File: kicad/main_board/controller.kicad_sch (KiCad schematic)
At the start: 44 parts, among them J6 FRONT_PANEL, J7 I2C, J8 SWD, U7 MCP4728, U8 RP2040, U9 W25Q128JVP, Y1 12MHz

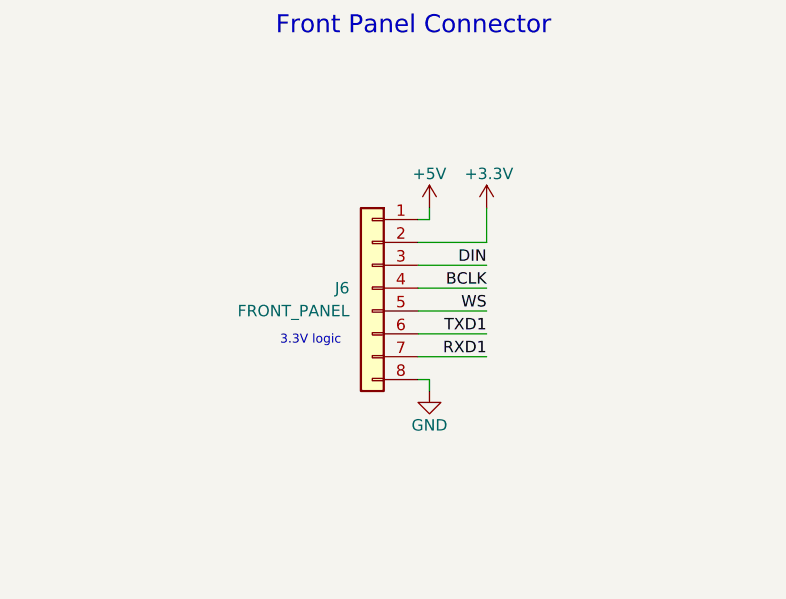
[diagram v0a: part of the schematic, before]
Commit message: use 2x4 IDC connector
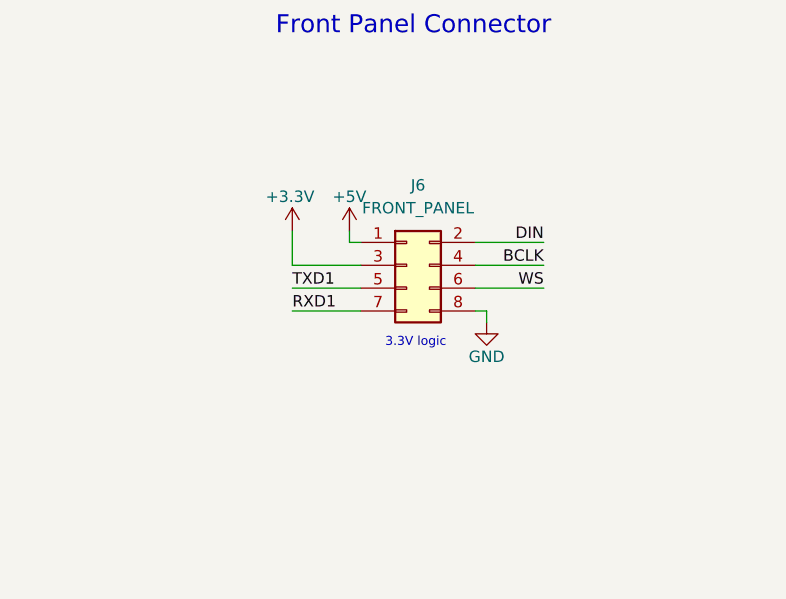
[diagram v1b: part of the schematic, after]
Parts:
- J6: footprint Connector_JST:JST_XH_B8B-XH-A_1x08_P2.50mm_Vertical -> Connector_IDC:IDC-Header_2x04_P2.54mm_Vertical; symbol Connector_Generic:Conn_01x08 -> Connector_Generic:Conn_02x04_Odd_Even; LCSC C7429638 -> C5372864
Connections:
- net +3.3V: now also J6.3 (Pin_3); no longer J6.2 (Pin_2)
- net DIN: now also J6.2 (Pin_2); no longer J6.3 (Pin_3)
- net TXD1: now also J6.5 (Pin_5); no longer J6.6 (Pin_6)
- net WS: now also J6.6 (Pin_6); no longer J6.5 (Pin_5)
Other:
- moved on the sheet: J6
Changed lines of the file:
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@@
 	(title_block
 		(title "SW32 - Main Board")
-		(date "2024-05-23")
+		(date "2024-05-29")
 		(rev "1")
 		(company "saawsm")
@@
 	(wire
 		(pts
-			(xy 58.42 45.72) (xy 58.42 46.99)
+			(xy 49.53 48.26) (xy 49.53 49.53)
 		)
 		(stroke
@@
 	(wire
 		(pts
-			(xy 64.77 45.72) (xy 64.77 49.53)
+			(xy 43.18 48.26) (xy 43.18 52.07)
 		)
 		(stroke
@@
 	(wire
 		(pts
-			(xy 57.15 62.23) (xy 64.77 62.23)
+			(xy 50.8 57.15) (xy 43.18 57.15)
 		)
 		(stroke
@@
 	(wire
 		(pts
-			(xy 57.15 57.15) (xy 64.77 57.15)
+			(xy 63.5 54.61) (xy 71.12 54.61)
 		)
 		(stroke
@@
 	(wire
 		(pts
-			(xy 64.77 49.53) (xy 57.15 49.53)
+			(xy 43.18 52.07) (xy 50.8 52.07)
 		)
 		(stroke
@@
 	(wire
 		(pts
-			(xy 57.15 52.07) (xy 64.77 52.07)
+			(xy 63.5 49.53) (xy 71.12 49.53)
 		)
 		(stroke
@@
 	(wire
 		(pts
-			(xy 57.15 54.61) (xy 64.77 54.61)
+			(xy 63.5 52.07) (xy 71.12 52.07)
 		)
 		(stroke
@@
 	(wire
 		(pts
-			(xy 58.42 64.77) (xy 58.42 66.04)
+			(xy 64.77 57.15) (xy 64.77 58.42)
 		)
 		(stroke
@@
 	(wire
 		(pts
-			(xy 57.15 59.69) (xy 64.77 59.69)
+			(xy 50.8 54.61) (xy 43.18 54.61)
 		)
 		(stroke
@@
 	(wire
 		(pts
-			(xy 58.42 64.77) (xy 57.15 64.77)
+			(xy 64.77 57.15) (xy 63.5 57.15)
 		)
 		(stroke
@@
 	(wire
 		(pts
-			(xy 57.15 46.99) (xy 58.42 46.99)
+			(xy 50.8 49.53) (xy 49.53 49.53)
 		)
 		(stroke
@@
 	(text "3.3V logic"
 		(exclude_from_sim no)
-		(at 45.212 60.452 0)
+		(at 56.896 60.706 0)
 		(effects
 			(font
@@
 	)
 	(label "WS"
-		(at 64.77 57.15 180)
+		(at 71.12 54.61 180)
 		(fields_autoplaced yes)
 		(effects
@@
 	)
 	(label "DIN"
-		(at 64.77 52.07 180)
+		(at 71.12 49.53 180)
 		(fields_autoplaced yes)
 		(effects
@@
 	)
 	(label "TXD1"
-		(at 64.77 59.69 180)
+		(at 43.18 54.61 0)
 		(fields_autoplaced yes)
 		(effects
@@
 				(size 1.27 1.27)
 			)
-			(justify right bottom)
+			(justify left bottom)
 		)
 	)
@@
 	)
 	(label "RXD1"
-		(at 64.77 62.23 180)
+		(at 43.18 57.15 0)
 		(fields_autoplaced yes)
 		(effects
@@
 				(size 1.27 1.27)
 			)
-			(justify right bottom)
+			(justify left bottom)
 		)
 	)
@@
 	)
 	(label "BCLK"
-		(at 64.77 54.61 180)
+		(at 71.12 52.07 180)
 		(fields_autoplaced yes)
 		(effects
@@
 	)
 	(symbol
-		(lib_id "Connector_Generic:Conn_01x08")
-		(at 52.07 54.61 0)
-		(mirror y)
+		(lib_id "Connector_Generic:Conn_02x04_Odd_Even")
+		(at 55.88 52.07 0)
 		(unit 1)
 		(exclude_from_sim no)
@@
 		(on_board yes)
 		(dnp no)
-		(fields_autoplaced yes)
 		(property "Reference" "J6"
-			(at 49.53 54.6099 0)
+			(at 57.15 43.18 0)
 			(effects
 				(font
 					(size 1.27 1.27)
 				)
-				(justify left)
 			)
 		)
 		(property "Value" "FRONT_PANEL"
-			(at 49.53 57.1499 0)
+			(at 57.15 45.72 0)
 			(effects
 				(font
 					(size 1.27 1.27)
 				)
-				(justify left)
 			)
 		)
-		(property "Footprint" "Connector_JST:JST_XH_B8B-XH-A_1x08_P2.50mm_Vertical"
-			(at 52.07 54.61 0)
+		(property "Footprint" "Connector_IDC:IDC-Header_2x04_P2.54mm_Vertical"
+			(at 55.88 52.07 0)
 			(effects
 				(font
@@
 			)
 		)
-		(property "Datasheet" "~"
-			(at 52.07 54.61 0)
+		(property "Datasheet" "https://www.lcsc.com/datasheet/lcsc_datasheet_2303141000_HCTL-HC-JN254-2-04-Z_C5372864.pdf"
+			(at 55.88 52.07 0)
 			(effects
 				(font
@@
 			)
 		)
-		(property "Description" "Generic connector, single row, 01x08, script generated (kicad-library-utils/schlib/autogen/connector/)"
-			(at 52.07 54.61 0)
+		(property "Description" "Generic connector, double row, 02x04, odd/even pin numbering scheme (row 1 odd numbers, row 2 even numbers), script generated (kicad-library-utils/schlib/autogen/connector/)"
+			(at 55.88 52.07 0)
 			(effects
 				(font
@@
 			)
 		)
-		(property "LCSC" "C7429638"
-			(at 52.07 54.61 0)
+		(property "LCSC" "C5372864"
+			(at 55.88 52.07 0)
 			(effects
 				(font
@@
 		)
 		(property "Service" "HandAssembly"
-			(at 52.07 54.61 0)
+			(at 55.88 52.07 0)
 			(effects
 				(font
@@
 	(symbol
 		(lib_id "power:+3.3V")
-		(at 64.77 45.72 0)
-		(mirror y)
+		(at 43.18 48.26 0)
 		(unit 1)
 		(exclude_from_sim no)
@@
 		(dnp no)
 		(property "Reference" "#PWR0102"
-			(at 64.77 49.53 0)
+			(at 43.18 52.07 0)
 			(effects
 				(font
@@
 		)
 		(property "Value" "+3.3V"
-			(at 65.024 41.91 0)
+			(at 42.926 44.45 0)
 			(effects
 				(font
@@
 		)
 		(property "Footprint" ""
-			(at 64.77 45.72 0)
+			(at 43.18 48.26 0)
 			(effects
 				(font
@@
 		)
 		(property "Datasheet" ""
-			(at 64.77 45.72 0)
+			(at 43.18 48.26 0)
 			(effects
 				(font
@@
 		)
 		(property "Description" "Power symbol creates a global label with name \"+3.3V\""
-			(at 64.77 45.72 0)
+			(at 43.18 48.26 0)
 			(effects
 				(font
@@
 	(symbol
 		(lib_id "power:+5V")
-		(at 58.42 45.72 0)
+		(at 49.53 48.26 0)
+		(mirror y)
 		(unit 1)
 		(exclude_from_sim no)
@@
 		(dnp no)
 		(property "Reference" "#PWR0100"
-			(at 58.42 49.53 0)
+			(at 49.53 52.07 0)
 			(effects
 				(font
@@
 		)
 		(property "Value" "+5V"
-			(at 58.42 41.91 0)
+			(at 49.53 44.45 0)
 			(effects
 				(font
@@
 		)
 		(property "Footprint" ""
-			(at 58.42 45.72 0)
+			(at 49.53 48.26 0)
 			(effects
 				(font
@@
 		)
 		(property "Datasheet" ""
-			(at 58.42 45.72 0)
+			(at 49.53 48.26 0)
 			(effects
 				(font
@@
 		)
 		(property "Description" "Power symbol creates a global label with name \"+5V\""
-			(at 58.42 45.72 0)
+			(at 49.53 48.26 0)
 			(effects
 				(font
@@
 	(symbol
 		(lib_id "power:GND")
-		(at 58.42 66.04 0)
+		(at 64.77 58.42 0)
 		(mirror y)
 		(unit 1)
@@
 		(dnp no)
 		(property "Reference" "#PWR0101"
-			(at 58.42 72.39 0)
+			(at 64.77 64.77 0)
 			(effects
 				(font
@@
 		)
 		(property "Value" "GND"
-			(at 58.42 69.85 0)
+			(at 64.77 62.23 0)
 			(effects
 				(font
@@
 		)
 		(property "Footprint" ""
-			(at 58.42 66.04 0)
+			(at 64.77 58.42 0)
 			(effects
 				(font
@@
 		)
 		(property "Datasheet" ""
-			(at 58.42 66.04 0)
+			(at 64.77 58.42 0)
 			(effects
 				(font
@@
 		)
 		(property "Description" "Power symbol creates a global label with name \"GND\" , ground"
-			(at 58.42 66.04 0)
+			(at 64.77 58.42 0)
 			(effects
 				(font

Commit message: connect charger VBUS before inrush limiter
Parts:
- renumbered R45 to R50, R46 to R51, R47 to R52, R48 to R53, R49 to R54, R50 to R55, R51 to R56, R52 to R57, R53 to R58, R54 to R59, R55 to R60, R56 to R61
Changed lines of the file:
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@@
 	(title_block
 		(title "SW32 - Main Board")
-		(date "2024-05-29")
+		(date "2024-05-31")
 		(rev "1")
 		(company "saawsm")
@@
 		(dnp no)
 		(fields_autoplaced yes)
-		(property "Reference" "R51"
+		(property "Reference" "R56"
 			(at 154.94 180.3399 0)
 			(effects
@@
 			(project "main_board"
 				(path "/8e1f1504-76c2-49e6-9261-3c1190503f8c/c17fbfa0-81d7-4817-8752-da6de21e6518"
-					(reference "R51")
+					(reference "R56")
 					(unit 1)
 				)
@@
 		(dnp no)
 		(fields_autoplaced yes)
-		(property "Reference" "R50"
+		(property "Reference" "R55"
 			(at 128.27 60.9599 0)
 			(effects
@@
 			(project "main_board"
 				(path "/8e1f1504-76c2-49e6-9261-3c1190503f8c/c17fbfa0-81d7-4817-8752-da6de21e6518"
-					(reference "R50")
+					(reference "R55")
 					(unit 1)
 				)
@@
 		(on_board yes)
 		(dnp no)
-		(property "Reference" "R45"
+		(property "Reference" "R50"
 			(at 41.148 146.05 0)
 			(effects
@@
 			(project "main_board"
 				(path "/8e1f1504-76c2-49e6-9261-3c1190503f8c/c17fbfa0-81d7-4817-8752-da6de21e6518"
-					(reference "R45")
+					(reference "R50")
 					(unit 1)
 				)
@@
 		(on_board yes)
 		(dnp no)
-		(property "Reference" "R55"
+		(property "Reference" "R60"
 			(at 270.51 42.926 90)
 			(effects
@@
 			(project "main_board"
 				(path "/8e1f1504-76c2-49e6-9261-3c1190503f8c/c17fbfa0-81d7-4817-8752-da6de21e6518"
-					(reference "R55")
+					(reference "R60")
 					(unit 1)
 				)
@@
 		(on_board yes)
 		(dnp no)
-		(property "Reference" "#PWR0102"
+		(property "Reference" "#PWR098"
 			(at 43.18 52.07 0)
 			(effects
@@
 			(project "main_board"
 				(path "/8e1f1504-76c2-49e6-9261-3c1190503f8c/c17fbfa0-81d7-4817-8752-da6de21e6518"
-					(reference "#PWR0102")
+					(reference "#PWR098")
 					(unit 1)
 				)
@@
 		(on_board yes)
 		(dnp no)
-		(property "Reference" "#PWR0100"
+		(property "Reference" "#PWR0101"
 			(at 49.53 52.07 0)
 			(effects
@@
 			(project "main_board"
 				(path "/8e1f1504-76c2-49e6-9261-3c1190503f8c/c17fbfa0-81d7-4817-8752-da6de21e6518"
-					(reference "#PWR0100")
+					(reference "#PWR0101")
 					(unit 1)
 				)
@@
 		(dnp no)
 		(fields_autoplaced yes)
-		(property "Reference" "R52"
+		(property "Reference" "R57"
 			(at 166.37 180.3399 0)
 			(effects
@@
 			(project "main_board"
 				(path "/8e1f1504-76c2-49e6-9261-3c1190503f8c/c17fbfa0-81d7-4817-8752-da6de21e6518"
-					(reference "R52")
+					(reference "R57")
 					(unit 1)
 				)
@@
 		(on_board yes)
 		(dnp no)
-		(property "Reference" "#PWR0101"
+		(property "Reference" "#PWR0102"
 			(at 64.77 64.77 0)
 			(effects
@@
 			(project "main_board"
 				(path "/8e1f1504-76c2-49e6-9261-3c1190503f8c/c17fbfa0-81d7-4817-8752-da6de21e6518"
-					(reference "#PWR0101")
+					(reference "#PWR0102")
 					(unit 1)
 				)
@@
 		(on_board yes)
 		(dnp no)
-		(property "Reference" "R53"
+		(property "Reference" "R58"
 			(at 207.01 52.07 0)
 			(effects
@@
 			(project "main_board"
 				(path "/8e1f1504-76c2-49e6-9261-3c1190503f8c/c17fbfa0-81d7-4817-8752-da6de21e6518"
-					(reference "R53")
+					(reference "R58")
 					(unit 1)
 				)
@@
 		(on_board yes)
 		(dnp no)
-		(property "Reference" "#PWR098"
+		(property "Reference" "#PWR099"
 			(at 46.99 181.61 0)
 			(effects
@@
 			(project "main_board"
 				(path "/8e1f1504-76c2-49e6-9261-3c1190503f8c/c17fbfa0-81d7-4817-8752-da6de21e6518"
-					(reference "#PWR098")
+					(reference "#PWR099")
 					(unit 1)
 				)
@@
 		(dnp no)
 		(fields_autoplaced yes)
-		(property "Reference" "R56"
+		(property "Reference" "R61"
 			(at 273.05 77.4699 0)
 			(effects
@@
 			(project "main_board"
 				(path "/8e1f1504-76c2-49e6-9261-3c1190503f8c/c17fbfa0-81d7-4817-8752-da6de21e6518"
-					(reference "R56")
+					(reference "R61")
 					(unit 1)
 				)
@@
 		(on_board yes)
 		(dnp no)
-		(property "Reference" "R49"
+		(property "Reference" "R54"
 			(at 124.46 79.502 90)
 			(effects
@@
 			(project "main_board"
 				(path "/8e1f1504-76c2-49e6-9261-3c1190503f8c/c17fbfa0-81d7-4817-8752-da6de21e6518"
-					(reference "R49")
+					(reference "R54")
 					(unit 1)
 				)
@@
 		(on_board yes)
 		(dnp no)
-		(property "Reference" "#PWR099"
+		(property "Reference" "#PWR0100"
 			(at 48.26 146.05 0)
 			(effects
@@
 			(project "main_board"
 				(path "/8e1f1504-76c2-49e6-9261-3c1190503f8c/c17fbfa0-81d7-4817-8752-da6de21e6518"
-					(reference "#PWR099")
+					(reference "#PWR0100")
 					(unit 1)
 				)
@@
 		(on_board yes)
 		(dnp no)
-		(property "Reference" "R54"
+		(property "Reference" "R59"
 			(at 262.89 119.126 90)
 			(effects
@@
 			(project "main_board"
 				(path "/8e1f1504-76c2-49e6-9261-3c1190503f8c/c17fbfa0-81d7-4817-8752-da6de21e6518"
-					(reference "R54")
+					(reference "R59")
 					(unit 1)
 				)
@@
 		(on_board yes)
 		(dnp no)
-		(property "Reference" "R46"
+		(property "Reference" "R51"
 			(at 49.53 168.9099 0)
 			(effects
@@
 			(project "main_board"
 				(path "/8e1f1504-76c2-49e6-9261-3c1190503f8c/c17fbfa0-81d7-4817-8752-da6de21e6518"
-					(reference "R46")
+					(reference "R51")
 					(unit 1)
 				)
@@
 		(on_board yes)
 		(dnp no)
-		(property "Reference" "R48"
+		(property "Reference" "R53"
 			(at 124.46 73.152 90)
 			(effects
@@
 			(project "main_board"
 				(path "/8e1f1504-76c2-49e6-9261-3c1190503f8c/c17fbfa0-81d7-4817-8752-da6de21e6518"
-					(reference "R48")
+					(reference "R53")
 					(unit 1)
 				)
@@
 		(on_board yes)
 		(dnp no)
-		(property "Reference" "R47"
+		(property "Reference" "R52"
 			(at 50.038 146.05 0)
 			(effects
@@
 			(project "main_board"
 				(path "/8e1f1504-76c2-49e6-9261-3c1190503f8c/c17fbfa0-81d7-4817-8752-da6de21e6518"
-					(reference "R47")
+					(reference "R52")
 					(unit 1)
 				)

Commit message: use 2x8 pin header
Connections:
- net CH1_GA: now also U8.6 (GPIO4); no longer U8.2 (GPIO0)
- net CH1_GB: now also U8.7 (GPIO5); no longer U8.3 (GPIO1)
- net CH2_GA: now also U8.2 (GPIO0); no longer U8.4 (GPIO2)
- net CH2_GB: now also U8.3 (GPIO1); no longer U8.5 (GPIO3)
- net CH3_GA: now also U8.4 (GPIO2); no longer U8.6 (GPIO4)
- net CH3_GB: now also U8.5 (GPIO3); no longer U8.7 (GPIO5)
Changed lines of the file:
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@@
 	(hierarchical_label "CH3_GB"
 		(shape output)
-		(at 190.5 82.55 0)
+		(at 190.5 77.47 0)
 		(fields_autoplaced yes)
 		(effects
@@
 	(hierarchical_label "CH2_GB"
 		(shape output)
-		(at 190.5 77.47 0)
+		(at 190.5 72.39 0)
 		(fields_autoplaced yes)
 		(effects
@@
 	(hierarchical_label "CH3_GA"
 		(shape output)
-		(at 190.5 80.01 0)
+		(at 190.5 74.93 0)
 		(fields_autoplaced yes)
 		(effects
@@
 	(hierarchical_label "CH1_GA"
 		(shape output)
-		(at 190.5 69.85 0)
+		(at 190.5 80.01 0)
 		(fields_autoplaced yes)
 		(effects
@@
 	(hierarchical_label "CH2_GA"
 		(shape output)
-		(at 190.5 74.93 0)
+		(at 190.5 69.85 0)
 		(fields_autoplaced yes)
 		(effects
@@
 	(hierarchical_label "CH1_GB"
 		(shape output)
-		(at 190.5 72.39 0)
+		(at 190.5 82.55 0)
 		(fields_autoplaced yes)
 		(effects
@@
 			)
 		)
-		(property "Datasheet" "~"
+		(property "Datasheet" "https://www.lcsc.com/datasheet/lcsc_datasheet_2201121800_XFCN-PZ254V-11-03P_C2937625.pdf"
 			(at 264.16 153.67 0)
 			(effects
@@
 			)
 		)
-		(property "Datasheet" "~"
+		(property "Datasheet" "https://www.lcsc.com/datasheet/lcsc_datasheet_2003141409_XFCN-PZ254V-11-02P_C492401.pdf"
 			(at 250.19 124.46 0)
 			(effects
@@
 			)
 		)
-		(property "Datasheet" "~"
+		(property "Datasheet" "https://www.lcsc.com/datasheet/lcsc_datasheet_2304140030_XFCN-PZ254V-11-04P_C2691448.pdf"
 			(at 127 180.34 0)
 			(effects
